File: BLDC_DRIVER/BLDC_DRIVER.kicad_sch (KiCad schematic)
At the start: 0 parts

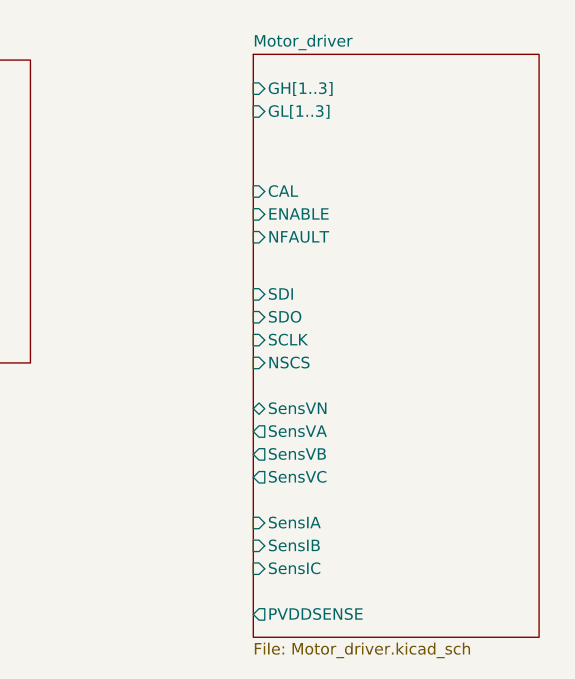
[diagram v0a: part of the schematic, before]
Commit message: added footprints, fault detection and temperature calc
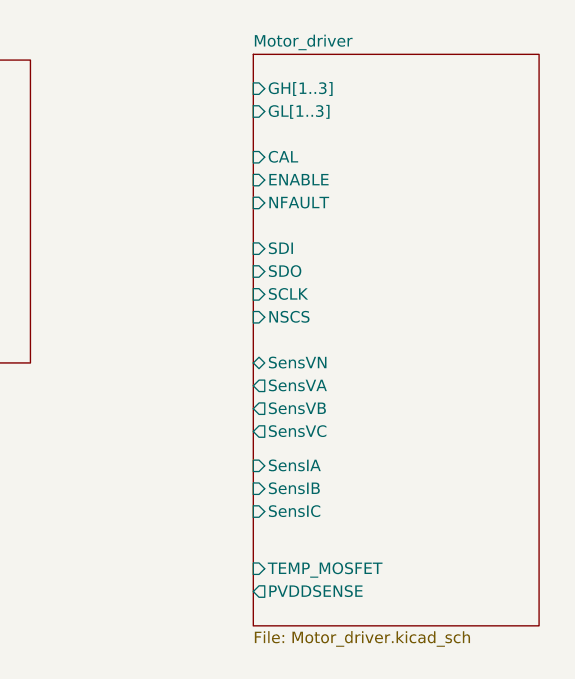
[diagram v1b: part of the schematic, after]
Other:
- sheet Motor_driver ports: added TEMP_MOSFET; removed none
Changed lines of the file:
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@@
 	(sheet
 		(at 157.48 36.83)
-		(size 31.75 64.77)
+		(size 31.75 63.5)
 		(exclude_from_sim no)
 		(in_bom yes)
@@
 		)
 		(property "Sheetfile" "Motor_driver.kicad_sch"
-			(at 157.48 102.1846 0)
+			(at 157.48 100.9146 0)
 			(effects
 				(font
@@
 		)
 		(pin "PVDDSENSE" output
-			(at 157.48 99.06 180)
+			(at 157.48 96.52 180)
 			(effects
 				(font
@@
 		)
 		(pin "SDO" input
+			(at 157.48 60.96 180)
+			(effects
+				(font
+					(size 1.27 1.27)
+				)
+				(justify left)
+			)
+		)
+		(pin "SCLK" input
+			(at 157.48 63.5 180)
+			(effects
+				(font
+					(size 1.27 1.27)
+				)
+				(justify left)
+			)
+		)
+		(pin "SensIA" input
+			(at 157.48 82.55 180)
+			(effects
+				(font
+					(size 1.27 1.27)
+				)
+				(justify left)
+			)
+		)
+		(pin "ENABLE" input
+			(at 157.48 50.8 180)
+			(effects
+				(font
+					(size 1.27 1.27)
+				)
+				(justify left)
+			)
+		)
+		(pin "CAL" input
+			(at 157.48 48.26 180)
+			(effects
+				(font
+					(size 1.27 1.27)
+				)
+				(justify left)
+			)
+		)
+		(pin "SensVB" output
+			(at 157.48 76.2 180)
+			(effects
+				(font
+					(size 1.27 1.27)
+				)
+				(justify left)
+			)
+		)
+		(pin "SensVC" output
+			(at 157.48 78.74 180)
+			(effects
+				(font
+					(size 1.27 1.27)
+				)
+				(justify left)
+			)
+		)
+		(pin "SensVA" output
+			(at 157.48 73.66 180)
+			(effects
+				(font
+					(size 1.27 1.27)
+				)
+				(justify left)
+			)
+		)
+		(pin "SensVN" bidirectional
+			(at 157.48 71.12 180)
+			(effects
+				(font
+					(size 1.27 1.27)
+				)
+				(justify left)
+			)
+		)
+		(pin "NFAULT" input
+			(at 157.48 53.34 180)
+			(effects
+				(font
+					(size 1.27 1.27)
+				)
+				(justify left)
+			)
+		)
+		(pin "SensIC" input
+			(at 157.48 87.63 180)
+			(effects
+				(font
+					(size 1.27 1.27)
+				)
+				(justify left)
+			)
+		)
+		(pin "SensIB" input
+			(at 157.48 85.09 180)
+			(effects
+				(font
+					(size 1.27 1.27)
+				)
+				(justify left)
+			)
+		)
+		(pin "NSCS" input
 			(at 157.48 66.04 180)
 			(effects
@@
 			)
 		)
-		(pin "SCLK" input
-			(at 157.48 68.58 180)
+		(pin "SDI" input
+			(at 157.48 58.42 180)
 			(effects
 				(font
@@
 			)
 		)
-		(pin "SensIA" input
-			(at 157.48 88.9 180)
-			(effects
-				(font
-					(size 1.27 1.27)
-				)
-				(justify left)
-			)
-		)
-		(pin "ENABLE" input
-			(at 157.48 54.61 180)
-			(effects
-				(font
-					(size 1.27 1.27)
-				)
-				(justify left)
-			)
-		)
-		(pin "CAL" input
-			(at 157.48 52.07 180)
-			(effects
-				(font
-					(size 1.27 1.27)
-				)
-				(justify left)
-			)
-		)
-		(pin "SensVB" output
-			(at 157.48 81.28 180)
-			(effects
-				(font
-					(size 1.27 1.27)
-				)
-				(justify left)
-			)
-		)
-		(pin "SensVC" output
-			(at 157.48 83.82 180)
-			(effects
-				(font
-					(size 1.27 1.27)
-				)
-				(justify left)
-			)
-		)
-		(pin "SensVA" output
-			(at 157.48 78.74 180)
-			(effects
-				(font
-					(size 1.27 1.27)
-				)
-				(justify left)
-			)
-		)
-		(pin "SensVN" bidirectional
-			(at 157.48 76.2 180)
-			(effects
-				(font
-					(size 1.27 1.27)
-				)
-				(justify left)
-			)
-		)
-		(pin "NFAULT" input
-			(at 157.48 57.15 180)
-			(effects
-				(font
-					(size 1.27 1.27)
-				)
-				(justify left)
-			)
-		)
-		(pin "SensIC" input
+		(pin "TEMP_MOSFET" input
 			(at 157.48 93.98 180)
 			(effects
 				(font
-					(size 1.27 1.27)
-				)
-				(justify left)
-			)
-		)
-		(pin "SensIB" input
-			(at 157.48 91.44 180)
-			(effects
-				(font
-					(size 1.27 1.27)
-				)
-				(justify left)
-			)
-		)
-		(pin "NSCS" input
-			(at 157.48 71.12 180)
-			(effects
-				(font
-					(size 1.27 1.27)
-				)
-				(justify left)
-			)
-		)
-		(pin "SDI" input
-			(at 157.48 63.5 180)
-			(effects
-				(font

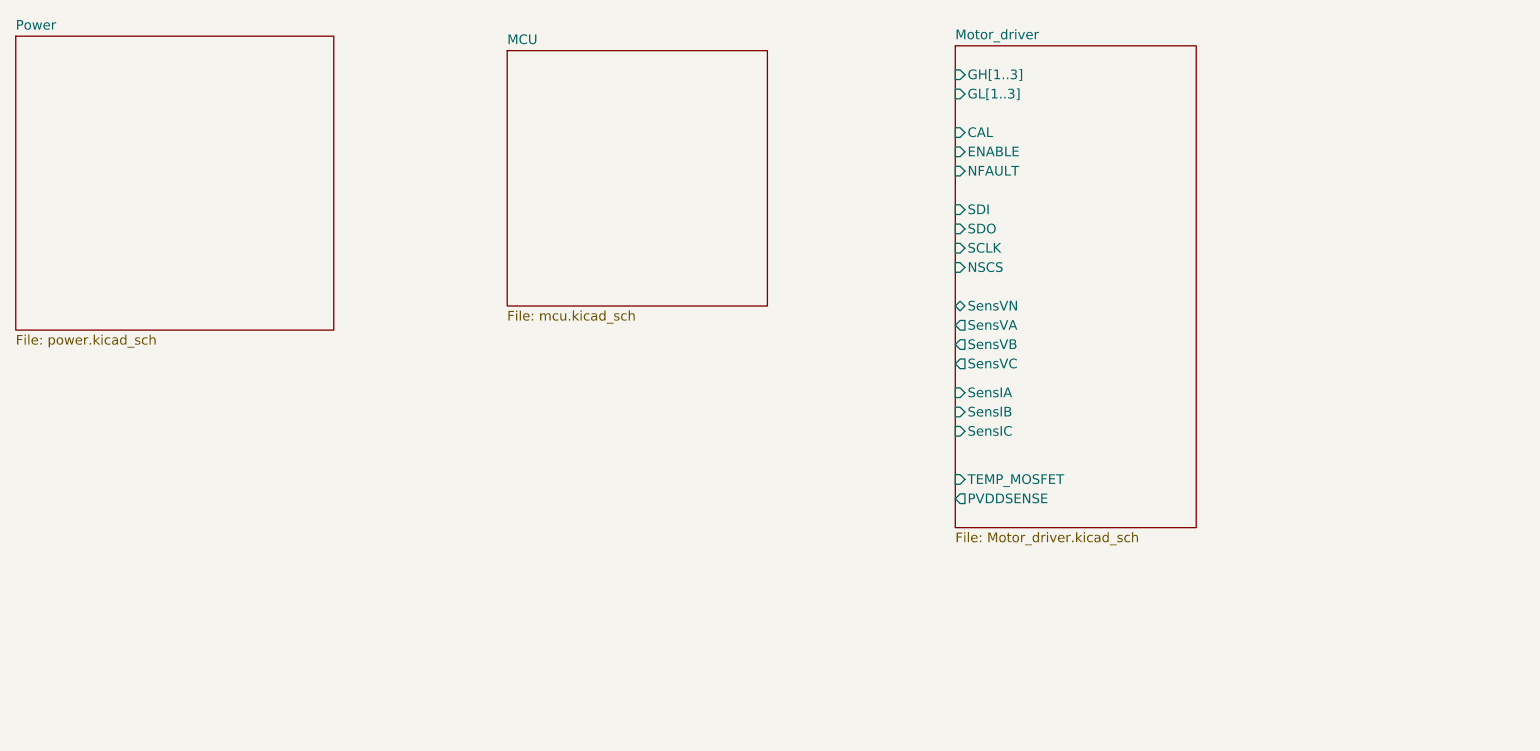
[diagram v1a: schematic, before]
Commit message: mcu added
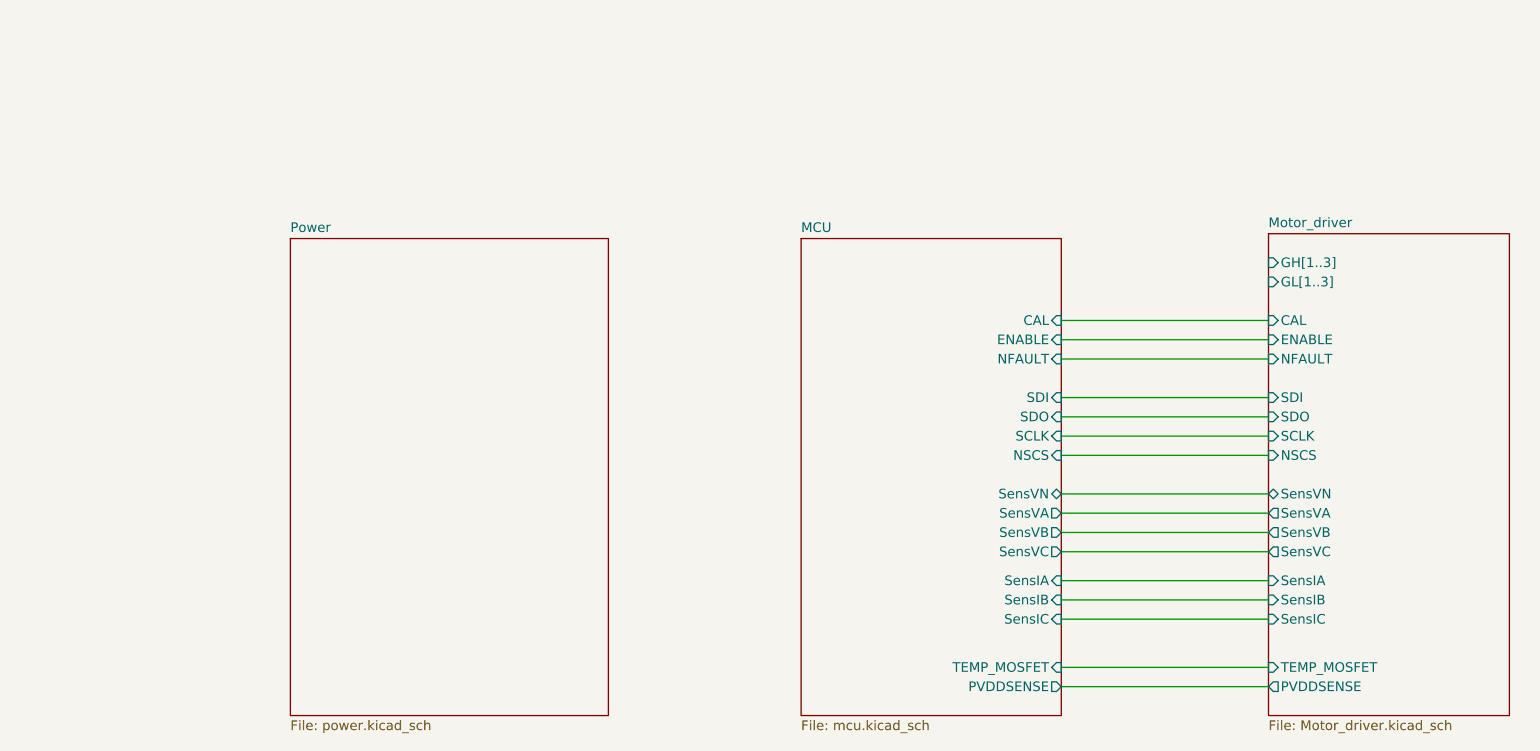
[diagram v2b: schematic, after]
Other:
- sheet MCU ports: added CAL, ENABLE, NFAULT, NSCS, PVDDSENSE, SCLK, SDI, SDO, SensIA, SensIB, SensIC, SensVA, SensVB, SensVC, SensVN, TEMP_MOSFET; removed none

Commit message: merge fix
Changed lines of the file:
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@@
 			)
 		)
-		(pin "SDO" input
+		(pin "SDO" output
 			(at 198.755 85.725 180)
 			(effects
@@
 			)
 		)
-		(pin "SensIA" input
+		(pin "SensIA" output
 			(at 198.755 107.315 180)
 			(effects
@@
 			)
 		)
-		(pin "SensVN" bidirectional
+		(pin "SensVN" output
 			(at 198.755 95.885 180)
 			(effects
@@
 			)
 		)
-		(pin "SensIC" input
+		(pin "SensIC" output
 			(at 198.755 112.395 180)
 			(effects
@@
 			)
 		)
-		(pin "SensIB" input
+		(pin "SensIB" output
 			(at 198.755 109.855 180)
 			(effects
@@
 			)
 		)
-		(pin "TEMP_MOSFET" input
+		(pin "TEMP_MOSFET" output
 			(at 198.755 118.745 180)
 			(effects
